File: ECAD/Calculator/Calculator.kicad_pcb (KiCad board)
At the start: 2 copper layers, 153.5 x 83.5 mm, 31 parts, among them SW1 Switch_Tactile_ESwitch, SW10 Switch_Tactile_ESwitch, SW11 Switch_Tactile_ESwitch, SW12 Switch_Tactile_ESwitch, SW13 Switch_Tactile_ESwitch, SW14 Switch_Tactile_ESwitch, SW15 Switch_Tactile_ESwitch, SW16 Switch_Tactile_ESwitch, SW17 Switch_Tactile_ESwitch, SW18 Switch_Tactile_ESwitch, SW19 Switch_Tactile_ESwitch, SW2 Switch_Tactile_ESwitch, SW20 Switch_Tactile_ESwitch, SW3 Switch_Tactile_ESwitch, SW4 Switch_Tactile_ESwitch, SW5 Switch_Tactile_ESwitch, SW6 Switch_Tactile_ESwitch, SW7 Switch_Tactile_ESwitch, SW8 Switch_Tactile_ESwitch, SW9 Switch_Tactile_ESwitch

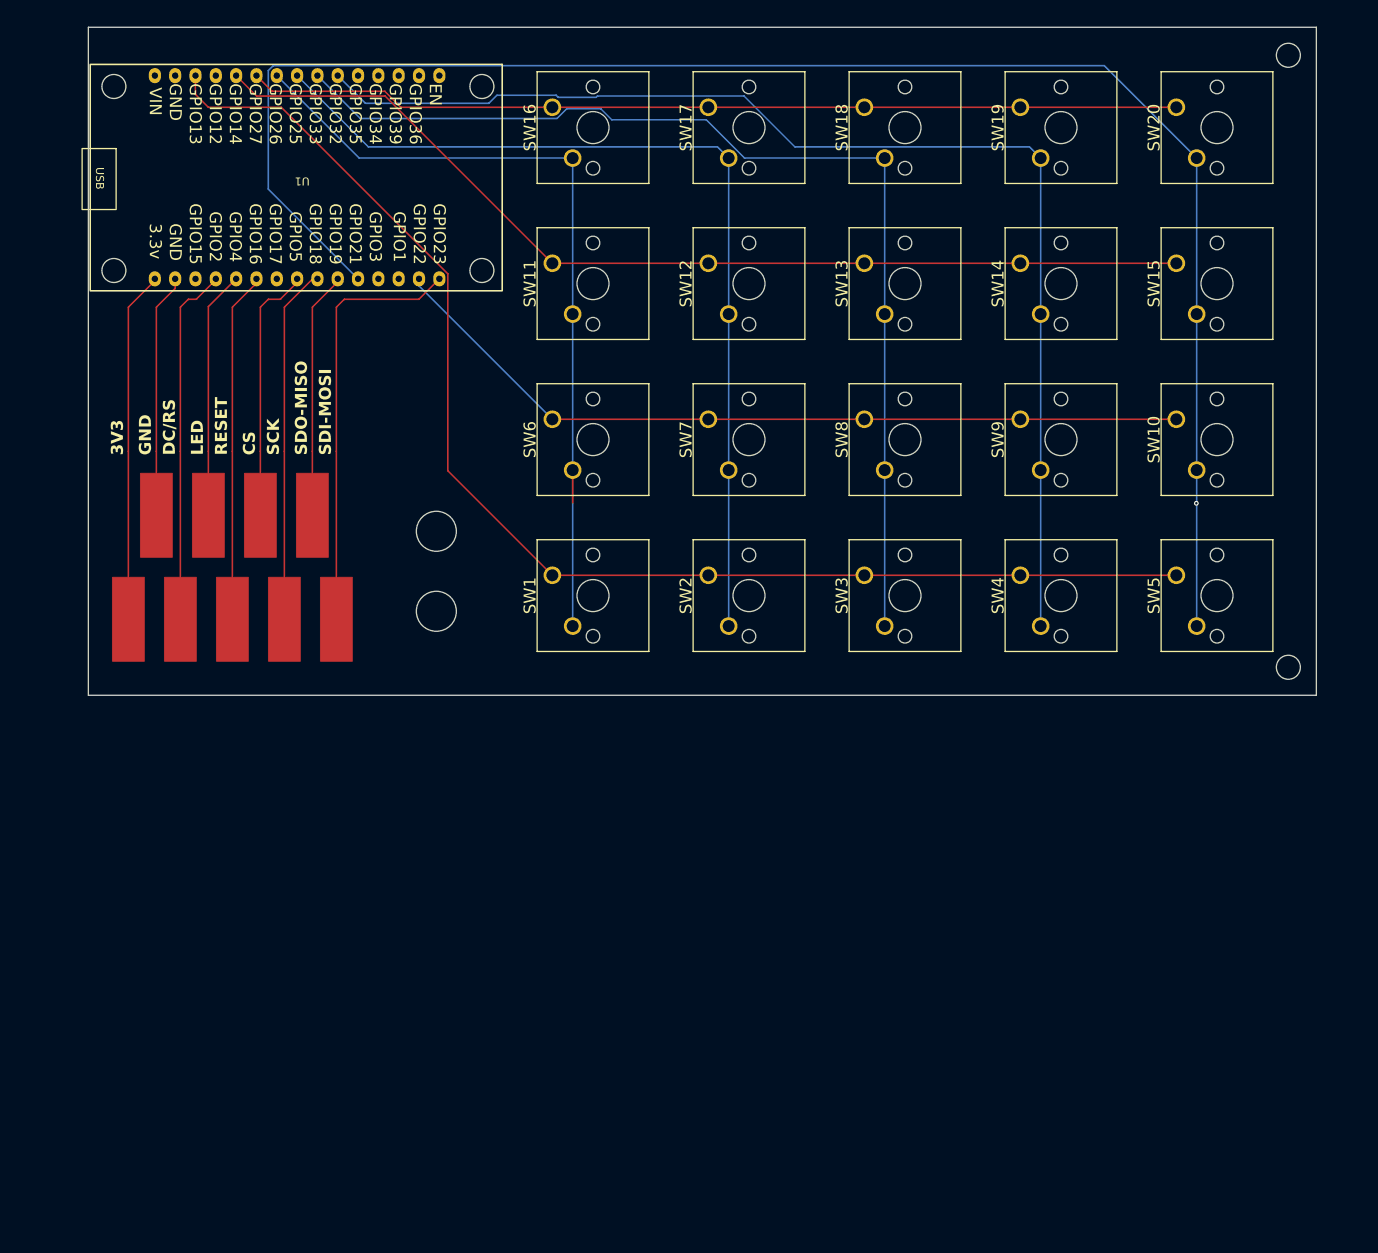
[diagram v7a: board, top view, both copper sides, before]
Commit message: Update ESP32_30pin footprint and add new MX-Solderable-1U footprint
- Updated ESP32_30pin.kicad_mod with new version, generator version, and 3D model
- Added new MX-Solderable-1U.kicad_mod footprint with detailed properties and pads.
- Introduced new 3D models for ESP32-30pin and Cherry MX switches.
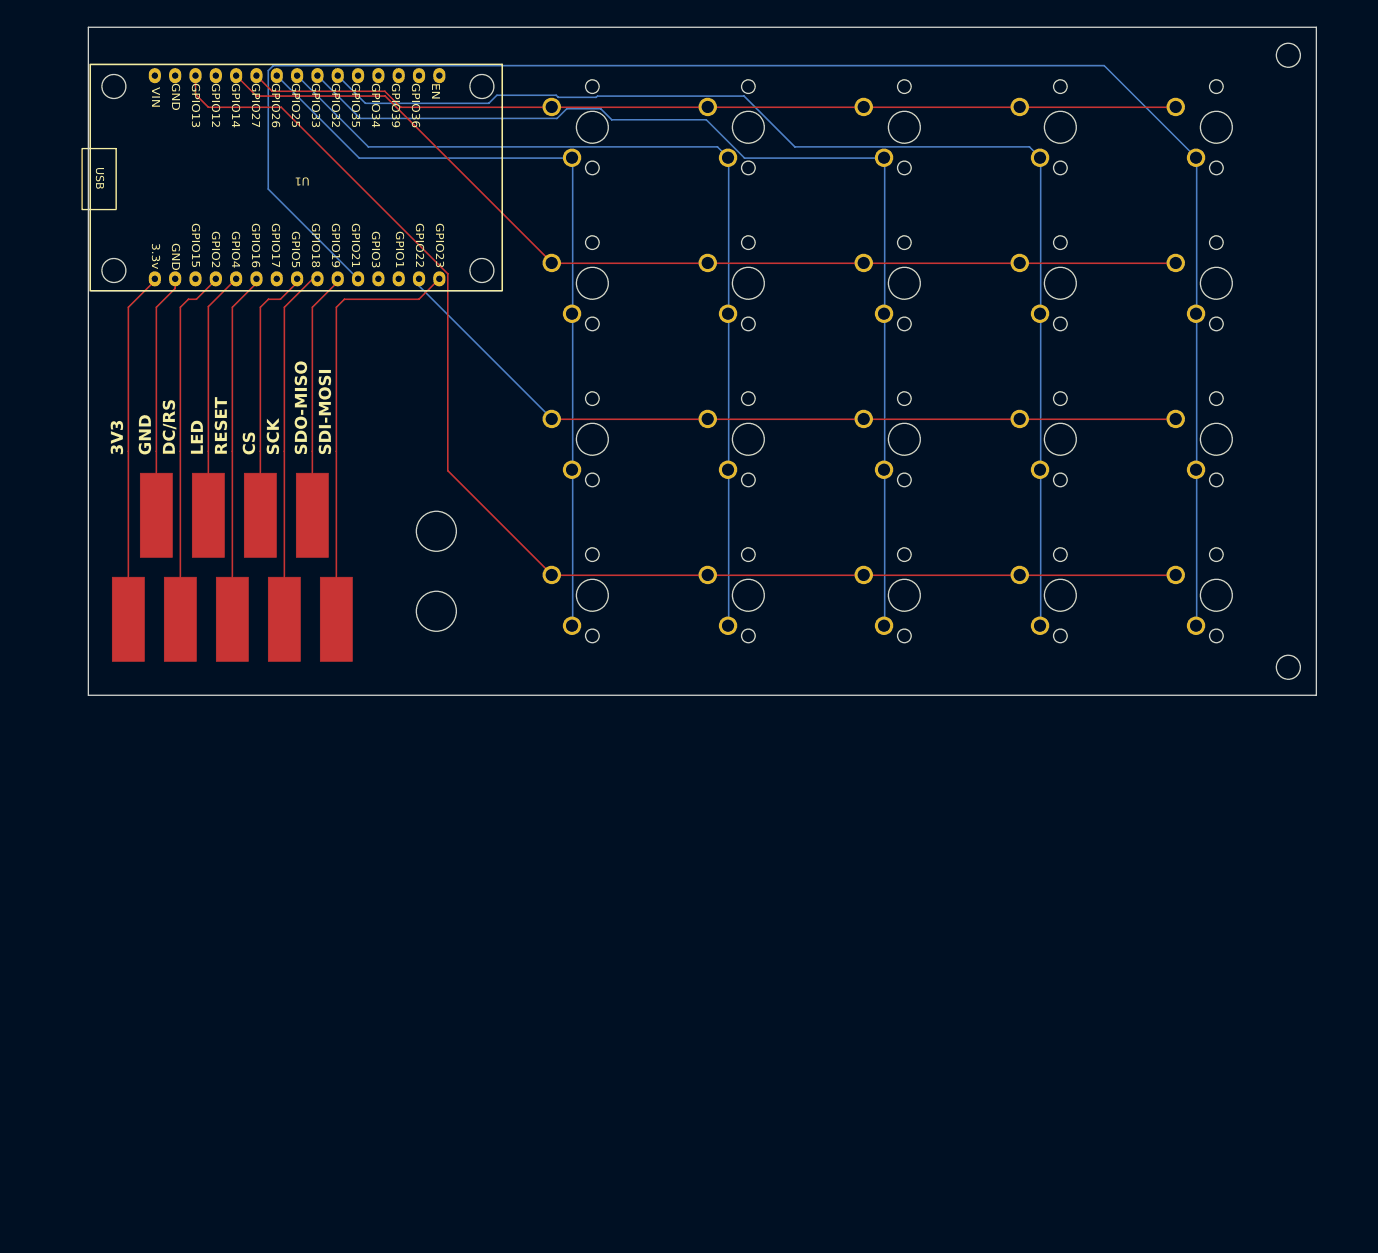
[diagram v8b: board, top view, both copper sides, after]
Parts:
- SW1, SW10, SW11, SW12, SW13, SW14, SW15, SW16, SW17, SW18, SW19, SW2, SW20, SW3, SW4, SW5, SW6, SW7, SW8, SW9: footprint Button_Switch_Keyboard:SW_Cherry_MX_1.00u_PCB -> Calculator_lib:MX-Solderable-1U
- U1: footprint ESP32_Footprints:ESP32_30pin -> Calculator_lib:ESP32_30pin
- moved SW1 5.59 mm to (89.5, 88.0)
- moved SW10 5.59 mm to (167.5, 68.5)
- moved SW11 5.59 mm to (89.5, 49.0)
- moved SW12 5.59 mm to (109.0, 49.0)
- moved SW13 5.59 mm to (128.5, 49.0)
- moved SW14 5.59 mm to (148.0, 49.0)
- moved SW15 5.59 mm to (167.5, 49.0)
- moved SW16 5.59 mm to (89.5, 29.5)
- moved SW17 5.59 mm to (109.0, 29.5)
- moved SW18 5.59 mm to (128.5, 29.5)
- moved SW19 5.59 mm to (148.0, 29.5)
- moved SW2 5.59 mm to (109.0, 88.0)
- moved SW20 5.59 mm to (167.5, 29.5)
- moved SW3 5.59 mm to (128.5, 88.0)
- moved SW4 5.59 mm to (148.0, 88.0)
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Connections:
- SW1 pad 1: /Col 1 -> /Row A
- SW1 pad 2: /Row A -> /Col 1
- SW10 pad 1: /Col 2 -> /Row E
- SW10 pad 2: /Row E -> /Col 2
- SW11 pad 1: /Col 3 -> /Row A
- SW11 pad 2: /Row A -> /Col 3
- SW12 pad 1: /Col 3 -> /Row B
- SW12 pad 2: /Row B -> /Col 3
- SW13 pad 1: /Col 3 -> /Row C
- SW13 pad 2: /Row C -> /Col 3
- SW14 pad 1: /Col 3 -> /Row D
- SW14 pad 2: /Row D -> /Col 3
- SW15 pad 1: /Col 3 -> /Row E
- SW15 pad 2: /Row E -> /Col 3
- SW16 pad 1: /Col 4 -> /Row A
- SW16 pad 2: /Row A -> /Col 4
- SW17 pad 1: /Col 4 -> /Row B
- SW17 pad 2: /Row B -> /Col 4
- SW18 pad 1: /Col 4 -> /Row C
- SW18 pad 2: /Row C -> /Col 4
- SW19 pad 1: /Col 4 -> /Row D
- SW19 pad 2: /Row D -> /Col 4
- SW2 pad 1: /Col 1 -> /Row B
- SW2 pad 2: /Row B -> /Col 1
- SW20 pad 1: /Col 4 -> /Row E
- SW20 pad 2: /Row E -> /Col 4
- SW3 pad 1: /Col 1 -> /Row C
- SW3 pad 2: /Row C -> /Col 1
- SW4 pad 1: /Col 1 -> /Row D
- SW4 pad 2: /Row D -> /Col 1
- SW5 pad 1: /Col 1 -> /Row E
- SW5 pad 2: /Row E -> /Col 1
- SW6 pad 1: /Col 2 -> /Row A
- SW6 pad 2: /Row A -> /Col 2
- SW7 pad 1: /Col 2 -> /Row B
- SW7 pad 2: /Row B -> /Col 2
- SW8 pad 1: /Col 2 -> /Row C
- SW8 pad 2: /Row C -> /Col 2
- SW9 pad 1: /Col 2 -> /Row D
- SW9 pad 2: /Row D -> /Col 2
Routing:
- net /Row A: track 103.9 -> 99.8 mm
- net /Row E: vias 1 -> 0
